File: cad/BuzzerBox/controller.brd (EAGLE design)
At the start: 100 x 100 mm, 143 parts, among them J2 RASPBERRYPI-40-PIN-GPIO_PTH_N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, Q1 BSS138, Q2 BSS138, Q3 BSS138, Q4 BSS138, Q5 BSS138, T1 BC849, T10 BC849, T2 BC849, T3 BC849, T4 BC849, T5 BC849, T6 BC849, T7 BC849, T8 BC849, T9 BC849, U1 ATMEGA328P-AU, Y1 16MHz

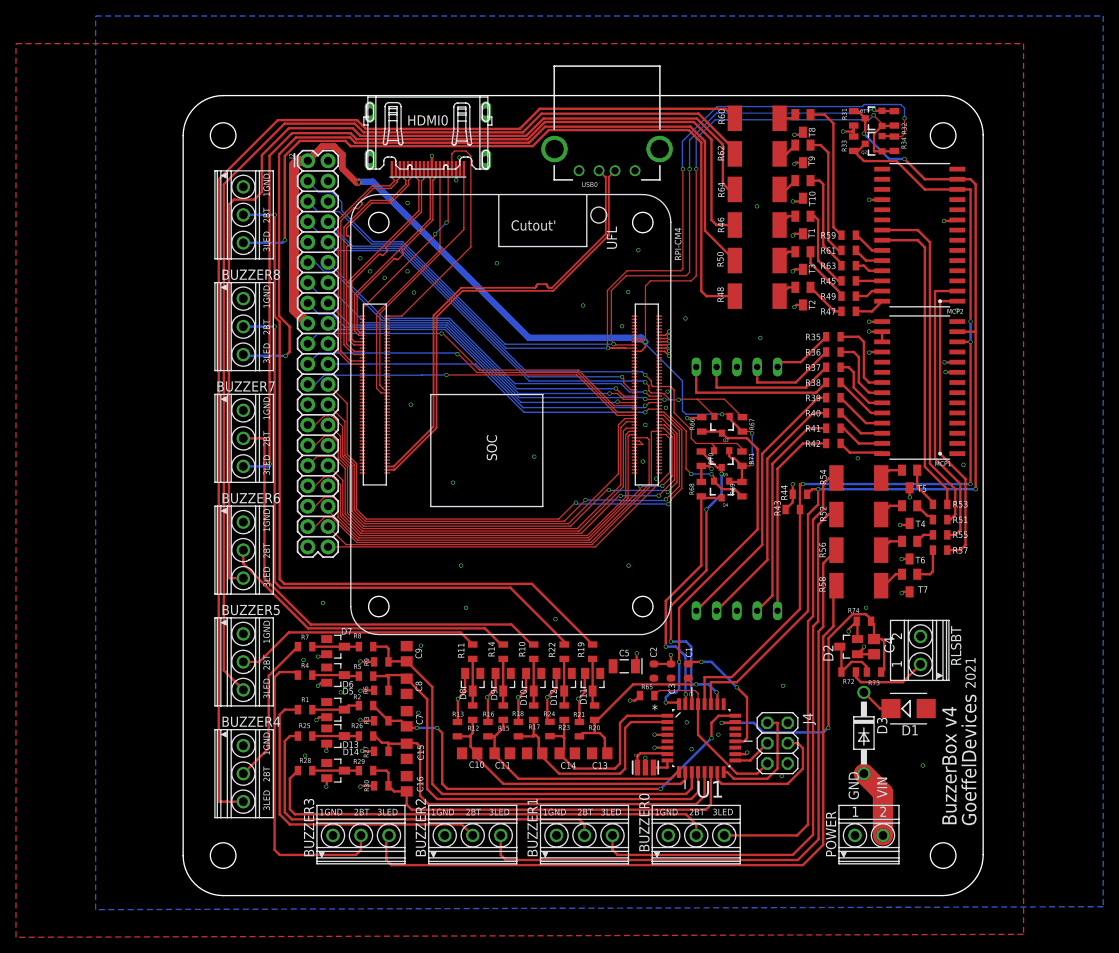
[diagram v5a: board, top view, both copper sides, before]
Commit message: Fix small pcb layout issues
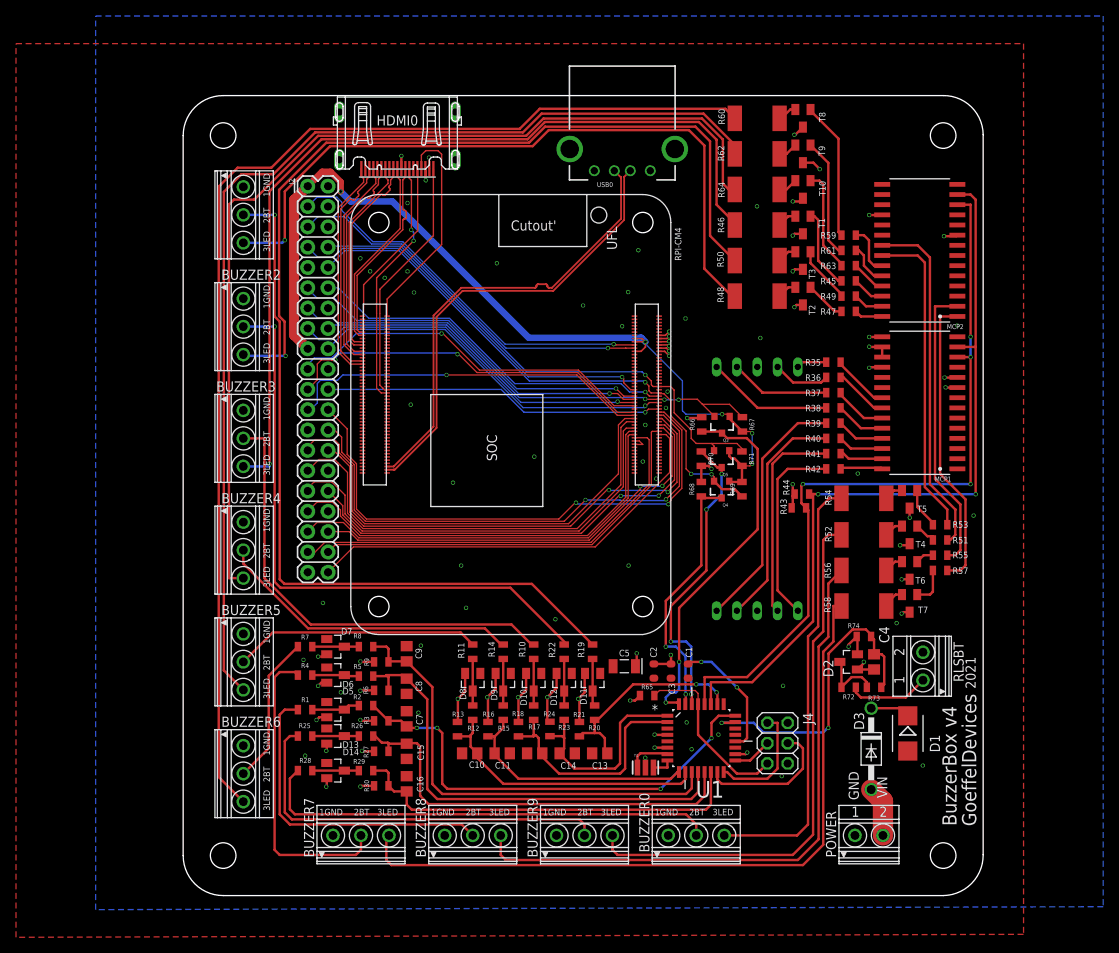
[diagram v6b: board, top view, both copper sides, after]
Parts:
- removed BUZZER1: 1751251, custom-350:1751251
- removed Q1, Q2: BSS138, SparkFun:SOT23-3
- removed R31, R32, R33, R34: 10K, SparkFun-Resistors:0805
- added BUZZER19: 1751251, custom-350:1751251
- moved BUZZER9 88.4 mm to (50.2, 7.62), turned to 0 degrees
- moved BUZZER2 69.6 mm to (7.62, 71.1), turned to 270 degrees
- moved BUZZER8 69.6 mm to (36.2, 7.62), turned to 0 degrees
- moved BUZZER3 51.6 mm to (7.62, 57.1), turned to 270 degrees
- moved BUZZER7 51.6 mm to (22.2, 7.62), turned to 0 degrees
- moved BUZZER4 27.9 mm to (7.62, 43.2)
- moved BUZZER6 27.9 mm to (7.62, 15.2)
- moved HDMI0 3.81 mm to (26.8, 94.8)
- moved R37 3.18 mm to (81.3, 62.9)
- moved R38 3.18 mm to (81.3, 61.0)
- moved R40 3.18 mm to (81.3, 57.1)
- moved R41 3.18 mm to (81.3, 55.2)
- moved J2 3.17 mm to (15.6, 88.7)
- moved R35 3.17 mm to (81.3, 66.7)
- moved R36 3.17 mm to (81.3, 64.8)
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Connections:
- net +3V3: no longer Q1.1, Q2.1, R32.2, R34.2
- net +5V: no longer R31.2, R33.2
- net GND: now also BUZZER19.1; no longer BUZZER1.1
- net LED0A2: now also BUZZER6.3; no longer BUZZER4.3
- net LED0A4: now also BUZZER4.3; no longer BUZZER6.3
- net LED0B0: now also BUZZER7.3; no longer BUZZER3.3
- net LED0B1: now also BUZZER8.3; no longer BUZZER2.3
- net LED1A0: now also BUZZER9.3; no longer BUZZER1.3
- net LED1A5: now also BUZZER3.3; no longer BUZZER7.3
- net LED1A6: now also BUZZER2.3; no longer BUZZER8.3
- net LED1A7: now also BUZZER19.3; no longer BUZZER9.3
- net N$23: now also BUZZER6.2; no longer BUZZER4.2
- net N$35: now also BUZZER7.2; no longer BUZZER3.2
- net N$36: now also BUZZER3.2; no longer BUZZER7.2
- net N$37: now also BUZZER19.2; no longer BUZZER9.2
- net N$38: now also BUZZER2.2; no longer BUZZER8.2
- net N$39: now also BUZZER9.2; no longer BUZZER1.2
- net N$4: now also BUZZER8.2; no longer BUZZER2.2
- net N$46: now also BUZZER4.2; no longer BUZZER6.2
- net SCL: no longer Q2.3, R33.1
- net SCLPI: no longer Q2.2, R34.1
- net SDA: no longer Q1.3, R31.1
- net SDAPI: no longer Q1.2, R32.1
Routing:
- net SCLPI: track 120.3 -> 48.2 mm, vias 3 -> 1
- net +3V3: track 177.9 -> 111.5 mm, vias 7 -> 5
- net SDAPI: track 111.3 -> 49.6 mm, vias 3 -> 1
- net SDA: track 116.4 -> 97.1 mm, vias 4 -> 2
- net SCL: track 112.7 -> 95.6 mm
- net LED1A7: track 93.5 -> 88.5 mm
- net F: track 12.1 -> 7.15 mm
- net A: track 17.3 -> 12.5 mm
- net LED1A5: track 113.9 -> 109.7 mm
- net B: track 20.0 -> 15.8 mm
- net G: track 7.65 -> 3.79 mm
- net LED0A2: track 150.4 -> 147.2 mm
- net LED1A6: track 103.7 -> 100.5 mm
- net GP13: track 56.6 -> 53.5 mm
- net GP12: track 60.2 -> 57.0 mm
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
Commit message: Start renaming resistors for better organization
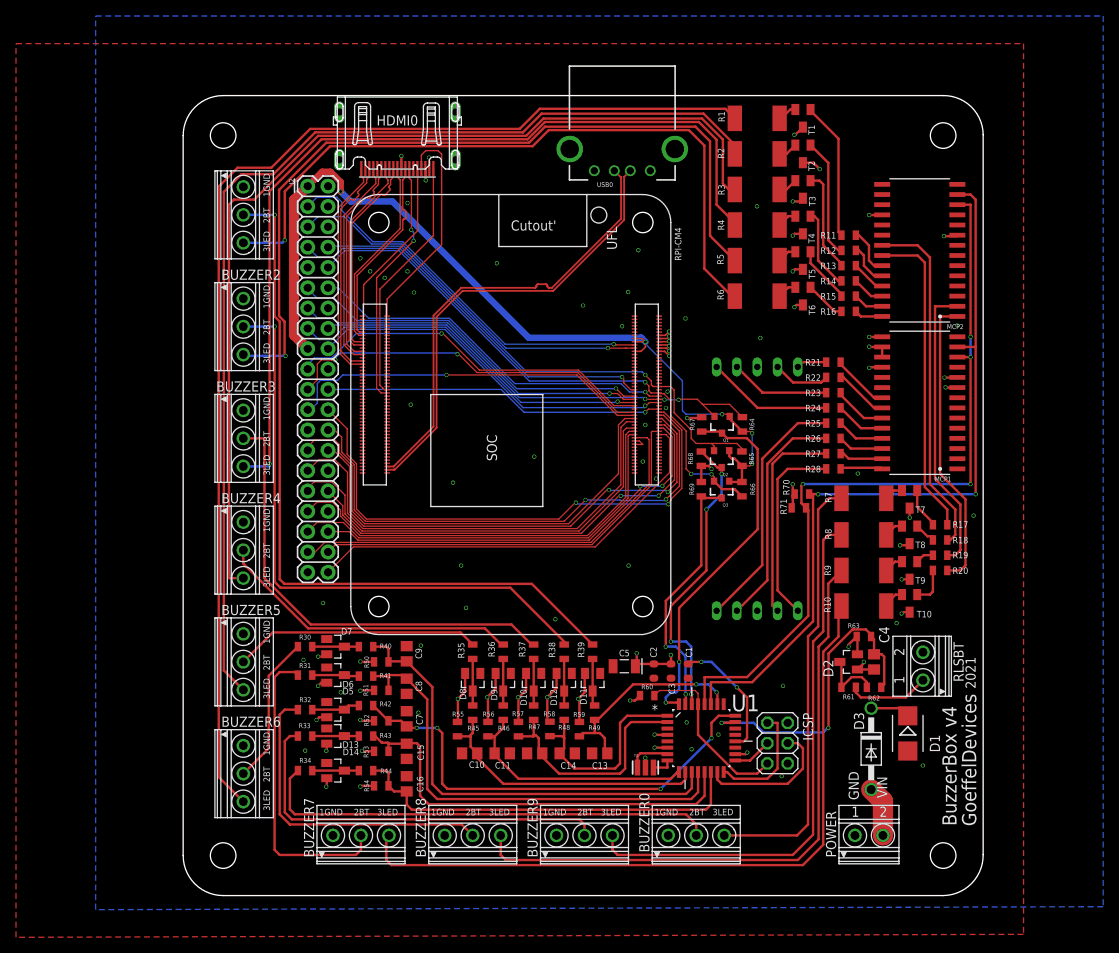
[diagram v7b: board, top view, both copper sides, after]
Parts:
- removed Q4: BSS138, SparkFun:SOT23-3
- removed R29, R73: 1k, SparkFun-Resistors:0805
- removed R72: 10, SparkFun-Resistors:0805
- removed R74: 100k, SparkFun-Resistors:0805
- added Q1: BSS138, SparkFun:SOT23-3
- added R31, R32, R33, R34: 10, SparkFun-Resistors:0805
- R1, R10, R4, R7: value 10 -> 50; device SparkFun-Resistors:0805 -> rcl:R2512
- R11, R14, R19: value 10 -> 1K
- R12, R15, R17, R20: value 1k -> 1K
- R13, R16, R18: value 100k -> 1K
- R2, R5, R8: value 1k -> 50; device SparkFun-Resistors:0805 -> rcl:R2512
- R21, R24, R27: value 100k -> 150
- R22, R25, R28: value 10 -> 150
- R23, R26: value 1k -> 150
- R3, R6, R9: value 100k -> 50; device SparkFun-Resistors:0805 -> rcl:R2512
- R30: value 100k -> 10
- R35, R36, R37, R38, R39: value 150 -> 10
- R40, R41, R42: value 150 -> 1k
- R43, R44: value (none) -> 1k
- R45, R47, R49: value 1K -> 1k
- R46, R48, R62: value 50 -> 1k; device rcl:R2512 -> SparkFun-Resistors:0805
- R50, R52, R54, R56, R58: value 50 -> 100k; device rcl:R2512 -> SparkFun-Resistors:0805
- R51, R53, R55, R57, R59, R63: value 1K -> 100k
- R60, R64: value 50 -> 10K; device rcl:R2512 -> SparkFun-Resistors:0805
- R61: value 1K -> 10
- R70, R71: value 10K -> (none)
- moved R1 93.0 mm to (71.8, 97.2)
- moved R2 84.5 mm to (71.8, 92.7)
- moved R3 81.4 mm to (71.8, 88.3), turned to 0 degrees
- moved R4 79.7 mm to (71.8, 83.8)
- moved R25 76.8 mm to (81.3, 59.1), turned to 180 degrees
- moved R28 76.1 mm to (81.3, 53.3), turned to 180 degrees
- moved R13 75.8 mm to (83.2, 78.7), turned to 180 degrees
- moved R53 75.4 mm to (24.8, 18.0)
- moved R12 74.5 mm to (83.2, 80.6), turned to 180 degrees
- moved R60 73.5 mm to (58.0, 25.0), turned to 180 degrees
- moved R51 72.3 mm to (24.8, 25.7)
- moved R7 72.3 mm to (85.1, 49.7)
- moved R45 71.6 mm to (36.2, 22.9), turned to 270 degrees
- moved R5 71.3 mm to (71.8, 79.4)
- moved R59 70.3 mm to (49.5, 20.8), turned to 90 degrees
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- renumbered J4 to ICSP, Q5 to Q2
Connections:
- net +3V3: now also Q1.1, R64.2, R65.2, R66.2; no longer Q4.1, R67.2, R69.2, R71.2
- net +5V: now also R50.2, R51.2, R52.2, R53.2, R54.2, R55.2, R56.2, R57.2, R58.2, R59.2, R60.2, R63.2, R67.2, R69.2, R71.2; no longer R13.2, R16.2, R18.2, R21.2, R24.2, R27.2, R3.2, R30.2, R43.2, R44.2, R6.2, R65.2, R66.2, R74.2, R9.2
- net A: now also R23.2; no longer R37.2
- net A0: now also R62.2, R63.1; no longer R73.2, R74.1
- net A1: now also R42.2, R52.1; no longer R2.2, R3.1
- net A3: now also R49.2, R59.1; no longer R20.2, R21.1
- net B: now also R24.2; no longer R38.2
- net C: now also R26.2; no longer R40.2
- net D: now also R27.2; no longer R41.2
- net D10: now also R44.2, R54.1; no longer R29.2, R30.1
- net D2: now also Q1.3, R67.1; no longer Q3.3, R66.1
- net D3: now also R48.2, R58.1; no longer R23.2, R24.1
- net D4: now also R47.2, R57.1; no longer R17.2, R18.1
- net D5: now also R46.2, R56.1; no longer R15.2, R16.1
- net D6: now also R45.2, R55.1; no longer R12.2, R13.1
- net D7: now also R40.2, R50.1; no longer R8.2, R9.1
- net D8: now also R41.2, R51.1; no longer R5.2, R6.1
- net D9: now also R43.2, R53.1; no longer R26.2, R27.1
- net DP: now also R25.2; no longer R39.2
- net E: now also R28.2; no longer R42.2
- net F: now also R22.2; no longer R36.2
- net G: now also R21.2; no longer R35.2
- net GP23: now also Q1.2, R64.1; no longer Q3.2, R67.1
- net GPA0: now also R18.1; no longer R51.1
- net GPA1: now also R17.1; no longer R53.1
- net GPA2: now also R11.1; no longer R59.1
- net GPA3: now also R12.1; no longer R61.1
- net GPA4: now also R13.1; no longer R63.1
- net GPA5: now also R14.1; no longer R45.1
- net GPA6: now also R15.1; no longer R49.1
- net GPA7: now also R16.1; no longer R47.1
- net GPB0: now also R20.1; no longer R57.1
- net GPB1: now also R19.1; no longer R55.1
- net LED0A2: now also R1.1; no longer R60.1
- net LED0A3: now also R2.1; no longer R62.1
- net LED0A4: now also R3.1; no longer R64.1
- net LED0B0: now also R10.1; no longer R58.1
- net LED0B1: now also R9.1; no longer R56.1
- net LED1A0: now also R8.1; no longer R52.1
- net LED1A1: now also R7.1; no longer R54.1
- net LED1A5: now also R4.1; no longer R46.1
- net LED1A6: now also R5.1; no longer R50.1
- net LED1A7: now also R6.1; no longer R48.1
- net N$1: now also R14.2, T4.1; no longer R45.2, T1.1
- net N$10: now also R15.2, T5.1; no longer R49.2, T3.1
- net N$11: now also R5.2, T5.2; no longer R50.2, T3.2
- net N$12: now also R35.2, R45.1; no longer R11.2, R12.1
- net N$13: now also R39.2, R49.1; no longer R19.2, R20.1
- net N$14: now also R18.2, T8.1; no longer R51.2, T4.1
- net N$15: now also R36.2, R46.1; no longer R14.2, R15.1
- net N$16: now also R8.2, T8.2; no longer R52.2, T4.2
- net N$17: now also R38.2, R48.1; no longer R22.2, R23.1
- net N$18: now also R17.2, T7.1; no longer R53.2, T5.1
- net N$19: now also R33.2, R43.1; no longer R25.2, R26.1
- net N$2: now also R4.2, T4.2; no longer R46.2, T1.2
- net N$20: now also R7.2, T7.2; no longer R54.2, T5.2
- net N$21: now also R19.2, T9.1; no longer R55.2, T6.1
- net N$22: now also R9.2, T9.2; no longer R56.2, T6.2
- net N$23: now also R30.1; no longer R7.1
- net N$24: now also R20.2, T10.1; no longer R57.2, T7.1
- net N$25: now also R10.2, T10.2; no longer R58.2, T7.2
- net N$26: now also R11.2, T1.1; no longer R59.2, T8.1
- net N$27: now also R1.2, T1.2; no longer R60.2, T8.2
- net N$28: now also R12.2, T2.1; no longer R61.2, T9.1
- net N$29: now also R2.2, T2.2; no longer R62.2, T9.2
- net N$3: now also R32.2, R42.1; no longer R1.2, R2.1
- net N$30: now also R13.2, T3.1; no longer R63.2, T10.1
- net N$31: now also R3.2, T3.2; no longer R64.2, T10.2
- net N$34: now also R34.2, R44.1; no longer R28.2, R29.1
- net N$35: now also R31.1; no longer R4.1
- net N$36: now also R37.1; no longer R10.1
- net N$37: now also R39.1; no longer R19.1
- net N$38: now also R38.1; no longer R22.1
- net N$39: now also R33.1; no longer R25.1
- net N$4: now also R32.1; no longer R1.1
- net N$40: now also R34.1; no longer R28.1
- net N$41: now also R61.2, R62.1; no longer R72.2, R73.1
- net N$45: now also R35.1; no longer R11.1
- net N$46: now also R36.1; no longer R14.1
- net N$5: now also R16.2, T6.1; no longer R47.2, T2.1
- net N$6: now also R31.2, R41.1; no longer R4.2, R5.1
- net N$7: now also R37.2, R47.1; no longer R10.2, R17.1
- net N$8: now also R6.2, T6.2; no longer R48.2, T2.2
- net N$9: now also R30.2, R40.1; no longer R7.2, R8.1
- net OA: now also R23.1; no longer R37.1
- net OB: now also R24.1; no longer R38.1
- net OC: now also R26.1; no longer R40.1
- net OD: now also R27.1; no longer R41.1
- net ODP: now also R25.1; no longer R39.1
- net OE: now also R28.1; no longer R42.1
- net OF: now also R22.1; no longer R36.1
- net OG: now also R21.1; no longer R35.1
- net RESET: now also R60.1; no longer R65.1
- net RLSBT: now also R61.1; no longer R72.1
- net RX: now also R68.1; no longer R70.1
- net RXD: now also Q3.2, R66.1; no longer Q4.2, R69.1
- net SCL: now also R71.1; no longer R43.1
- net SDA: now also R70.1; no longer R44.1
- net TX: now also Q3.3, R69.1; no longer Q4.3, R68.1
- net TXD: now also R65.1; no longer R71.1
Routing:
- net +5V: track 107.8 -> 110.0 mm

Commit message: Relabel components
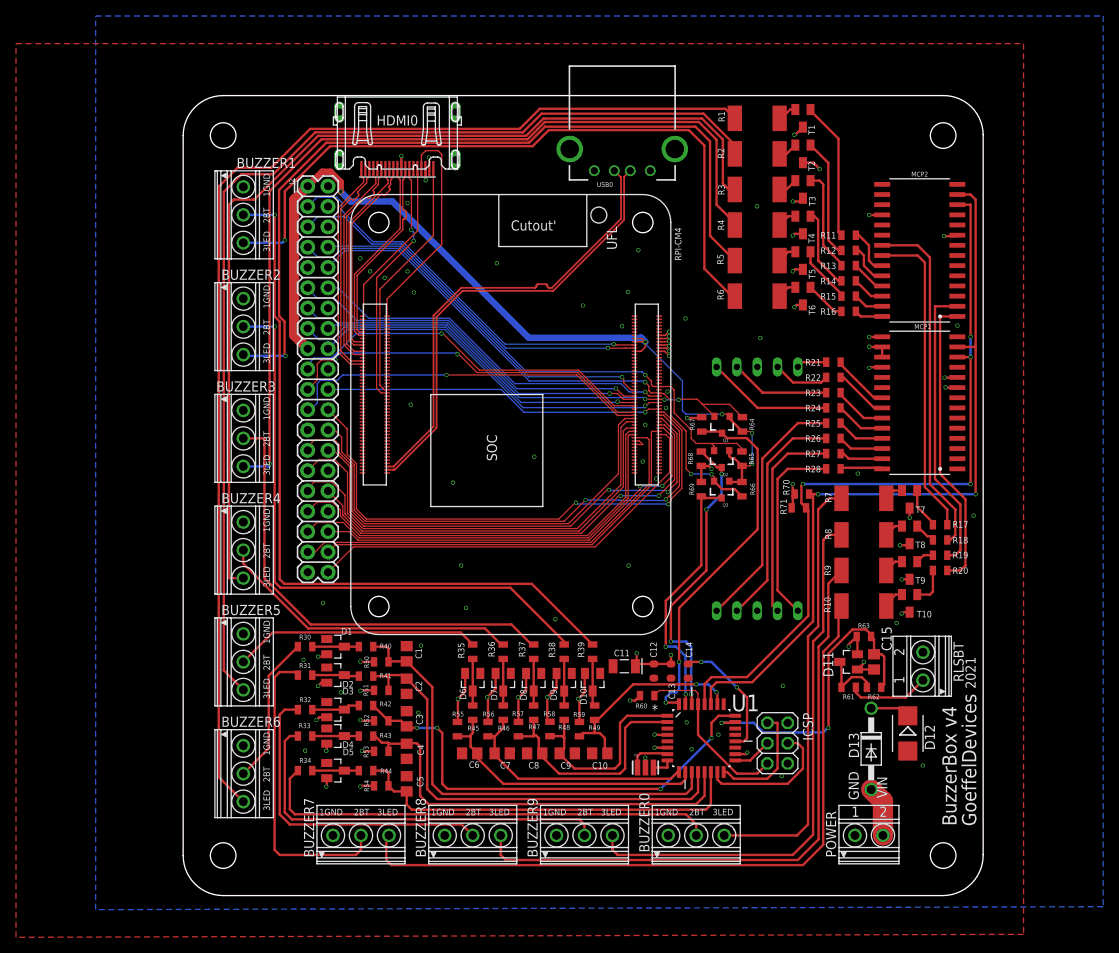
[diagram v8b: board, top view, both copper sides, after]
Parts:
- removed C16: 100nF, rcl:C0805
- removed D14: HSMS-2852, avago:SOT23
- added C6: 100nF, rcl:C0805
- added D4: HSMS-2852, avago:SOT23
- C1: device Condensatori:C0603-ROUND -> rcl:C0805
- C11: value 100nF -> 4,7uF_16V; device rcl:C0805 -> Condensatori:TAN-A
- C12, C13: value 100nF -> 1uF; device rcl:C0805 -> Condensatori:C0603-ROUND
- C14: device rcl:C0805 -> Condensatori:C0603-ROUND
- C2, C3: value 1uF -> 100nF; device Condensatori:C0603-ROUND -> rcl:C0805
- C5: value 4,7uF_16V -> 100nF; device Condensatori:TAN-A -> rcl:C0805
- D1: value (none) -> HSMS-2852; device diode:SMB -> avago:SOT23
- D12: value HSMS-2852 -> (none); device avago:SOT23 -> diode:SMB
- D13: value HSMS-2852 -> 1N4002; device avago:SOT23 -> diode:DO41-10
- D3: value 1N4002 -> HSMS-2852; device diode:DO41-10 -> avago:SOT23
- moved D1 72.3 mm to (19.1, 31.1)
- moved D3 67.1 mm to (19.1, 23.2)
- moved D13 67.0 mm to (86.0, 18.3)
- moved D2 64.2 mm to (19.1, 27.6), turned to 270 degrees
- moved C15 59.5 mm to (86.4, 29.2)
- moved C4 59.5 mm to (27.9, 18.0)
- moved D12 43.4 mm to (90.6, 20.3), turned to 270 degrees
- moved C1 35.2 mm to (27.9, 30.2), turned to 90 degrees
- moved C3 33.6 mm to (27.9, 22.1), turned to 90 degrees
- moved C5 32.1 mm to (27.9, 14.0), turned to 90 degrees
- moved D11 32.1 mm to (83.2, 29.2), turned to 90 degrees
- moved C2 31.0 mm to (27.9, 26.2)
- moved C9 23.6 mm to (48.0, 17.8), turned to 0 degrees
- moved D7 21.4 mm to (40.0, 26.7), turned to 180 degrees
- moved C11 19.9 mm to (56.5, 28.7), turned to 180 degrees
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- renumbered BUZZER19 to BUZZER1
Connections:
- net +5V: now also C11.1, C12.1, C13.1, D1.2, D12.C, D13.C, D3.2, D4.2; no longer C2.1, C3.1, C5.1, D1.C, D12.2, D13.2, D14.2, D3.C
- net A0: now also C15.1; no longer C4.1
- net A1: now also C3.1; no longer C7.1
- net A3: now also C10.1; no longer C13.1
- net D10: now also C5.1; no longer C16.1
- net D3: now also C9.1; no longer C14.1
- net D4: now also C8.1; no longer C12.1
- net D5: now also C7.1; no longer C11.1
- net D6: now also C6.1; no longer C10.1
- net D7: now also C1.1; no longer C9.1
- net D8: now also C2.1; no longer C8.1
- net D9: now also C4.1; no longer C15.1
- net GND: now also C6.2, D1.1, D12.A, D3.1, D4.1; no longer C16.2, D1.A, D12.1, D13.1, D14.1
- net N$12: now also D6.3; no longer D8.3
- net N$13: now also D10.3; no longer D11.3
- net N$15: now also D7.3; no longer D9.3
- net N$17: now also D9.3; no longer D12.3
- net N$19: now also D4.3; no longer D13.3
- net N$3: now also D3.3; no longer D5.3
- net N$32: now also D13.A; no longer D3.A
- net N$34: now also D5.3; no longer D14.3
- net N$41: now also D11.3; no longer D2.3
- net N$44: now also C14.1; no longer C1.1
- net N$6: now also D2.3; no longer D6.3
- net N$7: now also D8.3; no longer D10.3
- net N$9: now also D1.3; no longer D7.3
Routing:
- net SCL: track 95.6 -> 95.1 mm
